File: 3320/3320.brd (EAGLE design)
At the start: 57.8 x 216.2 mm, 70 parts, among them IC1 OPA2134P, IC2 OPA2134P, X1 2516-

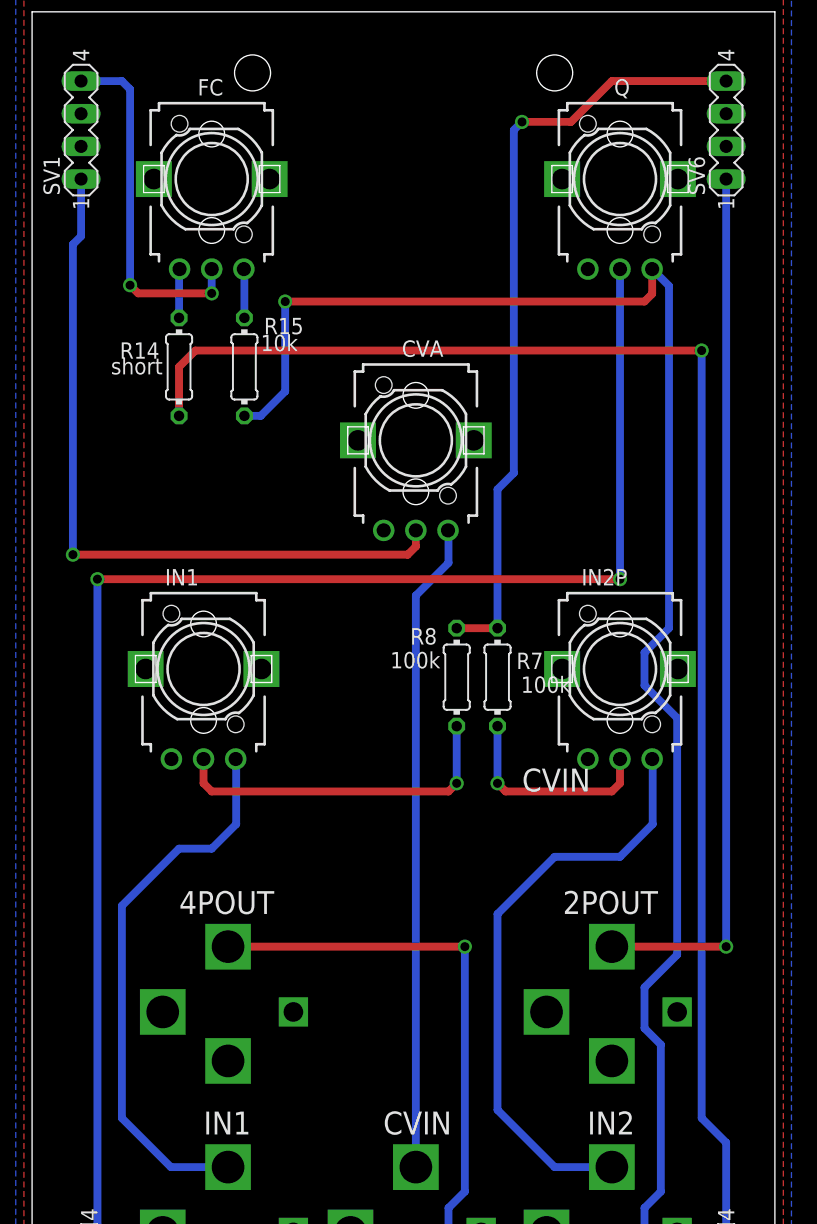
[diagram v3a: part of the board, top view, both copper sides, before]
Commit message: sent out vcf3 and 3320 for re spin
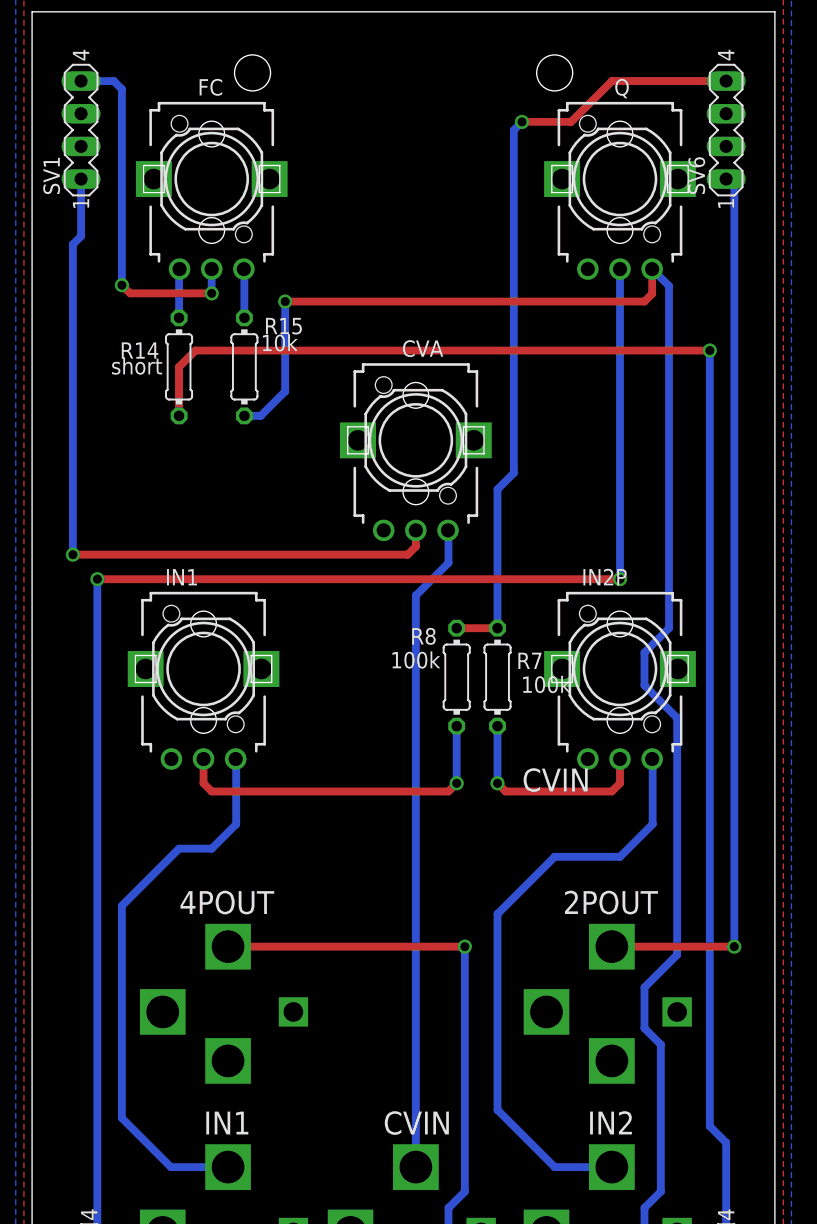
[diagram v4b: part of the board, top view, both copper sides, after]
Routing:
- net N$26: track 68.6 -> 69.5 mm
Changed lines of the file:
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@@
 <attribute name="VALUE" x="44.3992" y="31.4198" size="1.27" layer="21" font="vector" ratio="15"/>
 </element>
-<element name="IN1" library="dan" package="EVUFXJ" value="US-EVUF2J" x="13.335" y="165.1"/>
-<element name="IN2P" library="dan" package="EVUFXJ" value="US-EVUF2J" x="45.72" y="165.1"/>
+<element name="IN1" library="dan" package="EVUFXJ" value="US-EVUF2J" x="13.335" y="165.1" smashed="yes">
+<attribute name="NAME" x="10.335" y="171.6" size="1.27" layer="21"/>
+</element>
+<element name="IN2P" library="dan" package="EVUFXJ" value="US-EVUF2J" x="45.72" y="165.1" smashed="yes">
+<attribute name="NAME" x="42.72" y="171.6" size="1.27" layer="21"/>
+</element>
 </elements>
 <signals>
@@
 <contactref element="IC2" pad="4"/>
 <wire x1="53.975" y1="120.65" x2="53.975" y2="128.27" width="0.6096" layer="16"/>
-<wire x1="53.975" y1="128.27" x2="52.07" y2="130.175" width="0.6096" layer="16"/>
-<wire x1="52.07" y1="130.175" x2="52.07" y2="189.865" width="0.6096" layer="16"/>
-<via x="52.07" y="189.865" extent="1-16" drill="0.7"/>
+<wire x1="53.975" y1="128.27" x2="52.705" y2="129.54" width="0.6096" layer="16"/>
+<wire x1="52.705" y1="129.54" x2="52.705" y2="189.865" width="0.6096" layer="16"/>
+<via x="52.705" y="189.865" extent="1-16" drill="0.7"/>
 <contactref element="R27" pad="2"/>
 <contactref element="R26" pad="2"/>
@@
 <via x="41.275" y="12.065" extent="1-16" drill="0.7"/>
 <wire x1="41.275" y1="12.065" x2="45.085" y2="12.065" width="0.6096" layer="1"/>
-<wire x1="52.07" y1="189.865" x2="12.7" y2="189.865" width="0.6096" layer="1"/>
+<wire x1="52.705" y1="189.865" x2="12.7" y2="189.865" width="0.6096" layer="1"/>
 <wire x1="12.7" y1="189.865" x2="11.43" y2="188.595" width="0.6096" layer="1"/>
 <wire x1="11.43" y1="188.595" x2="11.43" y2="184.785" width="0.6096" layer="1"/>
@@
 <wire x1="13.97" y1="196.2" x2="13.97" y2="194.31" width="0.6096" layer="16"/>
 <via x="13.97" y="194.31" extent="1-16" drill="0.7"/>
-<wire x1="13.97" y1="194.31" x2="8.255" y2="194.31" width="0.6096" layer="1"/>
-<wire x1="8.255" y1="194.31" x2="7.62" y2="194.945" width="0.6096" layer="1"/>
-<via x="7.62" y="194.945" extent="1-16" drill="0.7"/>
-<wire x1="7.62" y1="194.945" x2="7.62" y2="210.185" width="0.6096" layer="16"/>
-<wire x1="7.62" y1="210.185" x2="6.985" y2="210.82" width="0.6096" layer="16"/>
-<wire x1="6.985" y1="210.82" x2="3.81" y2="210.82" width="0.6096" layer="16"/>
+<wire x1="13.97" y1="194.31" x2="7.62" y2="194.31" width="0.6096" layer="1"/>
+<wire x1="7.62" y1="194.31" x2="6.985" y2="194.945" width="0.6096" layer="1"/>
+<via x="6.985" y="194.945" extent="1-16" drill="0.7"/>
+<wire x1="6.985" y1="194.945" x2="6.985" y2="210.185" width="0.6096" layer="16"/>
+<wire x1="6.985" y1="210.185" x2="6.35" y2="210.82" width="0.6096" layer="16"/>
+<wire x1="6.35" y1="210.82" x2="3.81" y2="210.82" width="0.6096" layer="16"/>
 </signal>
 <signal name="N$17">
@@
 <contactref element="SV6" pad="1"/>
 <contactref element="2POUT" pad="P$3"/>
-<wire x1="53.975" y1="203.2" x2="53.975" y2="143.51" width="0.6096" layer="16"/>
-<via x="53.975" y="143.51" extent="1-16" drill="0.7"/>
-<wire x1="53.975" y1="143.51" x2="45.085" y2="143.51" width="0.6096" layer="1"/>
+<via x="54.61" y="143.51" extent="1-16" drill="0.7"/>
+<wire x1="54.61" y1="143.51" x2="45.085" y2="143.51" width="0.6096" layer="1"/>
+<wire x1="54.61" y1="143.51" x2="54.61" y2="202.565" width="0.6096" layer="16"/>
+<wire x1="54.61" y1="202.565" x2="53.975" y2="203.2" width="0.6096" layer="16"/>
 </signal>
 <signal name="N$28">

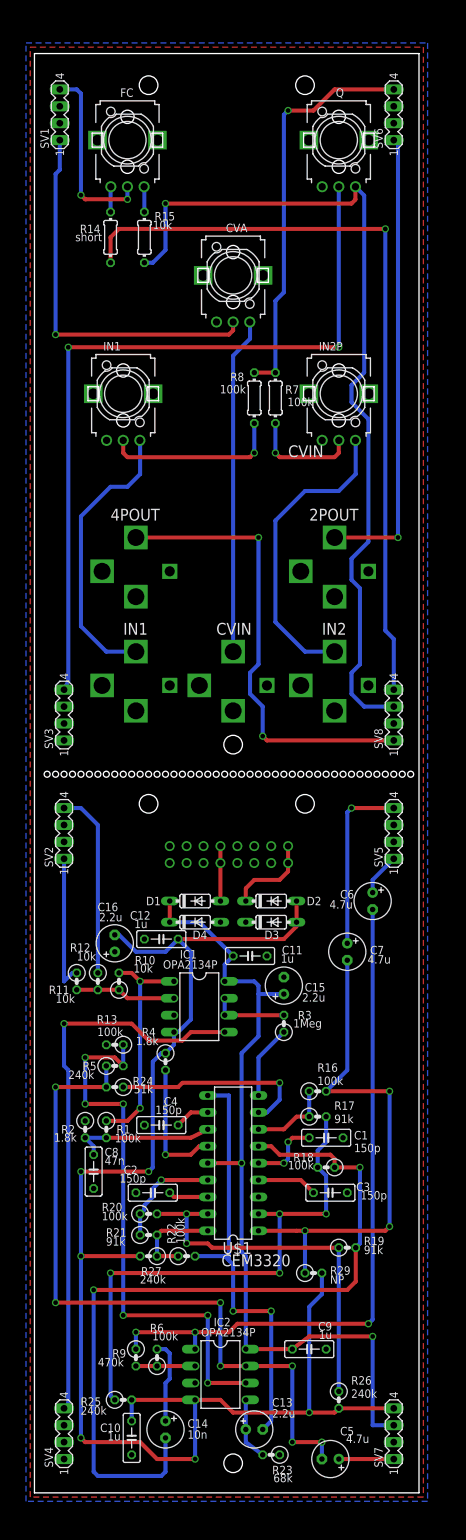
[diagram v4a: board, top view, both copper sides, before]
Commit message: made post fab component changes to 3320 and some fixes to svf board
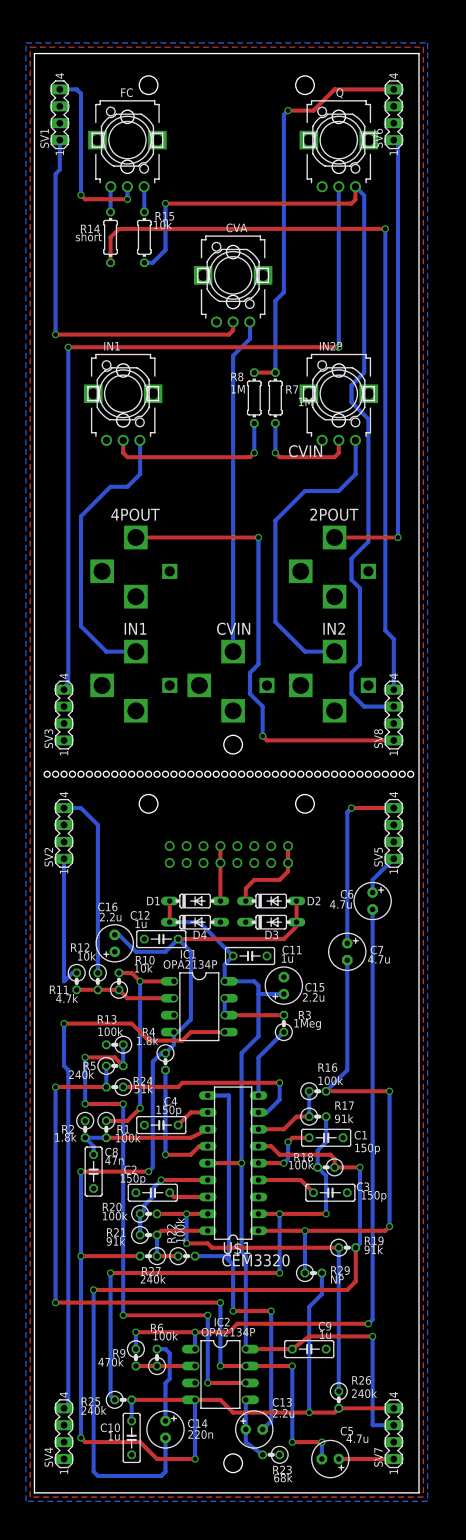
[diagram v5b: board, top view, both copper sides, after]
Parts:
- C14: value 10n -> 220n
- R11: value 10k -> 4.7k
- R7, R8: value 100k -> 1M
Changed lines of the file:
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@@
 <attribute name="VALUE" x="17.78" y="79.4258" size="1.27" layer="21" font="vector" ratio="15" rot="R180"/>
 </element>
-<element name="R11" library="dan" package="0207/2V" value="10k" x="6.35" y="76.835" smashed="yes" rot="R270">
+<element name="R11" library="dan" package="0207/2V" value="4.7k" x="6.35" y="76.835" smashed="yes" rot="R270">
 <attribute name="NAME" x="2.159" y="74.93" size="1.27" layer="21" font="vector" ratio="15"/>
 <attribute name="VALUE" x="3.175" y="73.6092" size="1.27" layer="21" font="vector" ratio="15"/>
@@
 <attribute name="VALUE" x="21.59" y="24.1808" size="1.27" layer="21" font="vector" ratio="15" rot="R180"/>
 </element>
-<element name="R7" library="dan" package="0204/7" value="100k" x="36.195" y="164.465" smashed="yes" rot="R90">
+<element name="R7" library="dan" package="0204/7" value="1M" x="36.195" y="164.465" smashed="yes" rot="R90">
 <attribute name="NAME" x="39.751" y="166.37" size="1.27" layer="21" font="vector" ratio="15" rot="R180"/>
 <attribute name="VALUE" x="41.91" y="164.5158" size="1.27" layer="21" font="vector" ratio="15" rot="R180"/>
 </element>
-<element name="R8" library="dan" package="0204/7" value="100k" x="33.02" y="164.465" smashed="yes" rot="R90">
+<element name="R8" library="dan" package="0204/7" value="1M" x="33.02" y="164.465" smashed="yes" rot="R90">
 <attribute name="NAME" x="31.496" y="168.275" size="1.27" layer="21" font="vector" ratio="15" rot="R180"/>
 <attribute name="VALUE" x="31.75" y="166.4208" size="1.27" layer="21" font="vector" ratio="15" rot="R180"/>
@@
 <attribute name="VALUE" x="19.7358" y="32.7152" size="1.27" layer="21" font="vector" ratio="15" rot="R180"/>
 </element>
-<element name="C14" library="dan" package="E2,5-6" value="10n" x="19.685" y="9.525" smashed="yes" rot="R270">
+<element name="C14" library="dan" package="E2,5-6" value="220n" x="19.685" y="9.525" smashed="yes" rot="R270">
 <attribute name="NAME" x="22.987" y="9.779" size="1.27" layer="21" font="vector" ratio="15"/>
 <attribute name="VALUE" x="22.987" y="8.128" size="1.27" layer="21" font="vector" ratio="15"/>

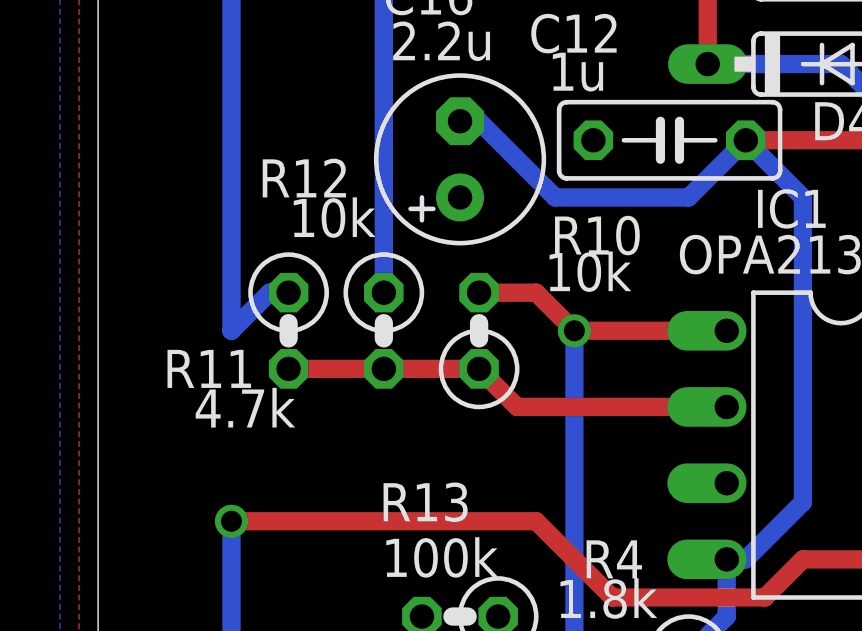
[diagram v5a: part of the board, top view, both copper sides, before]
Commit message: respun the svf.  changed a few components on the 3320
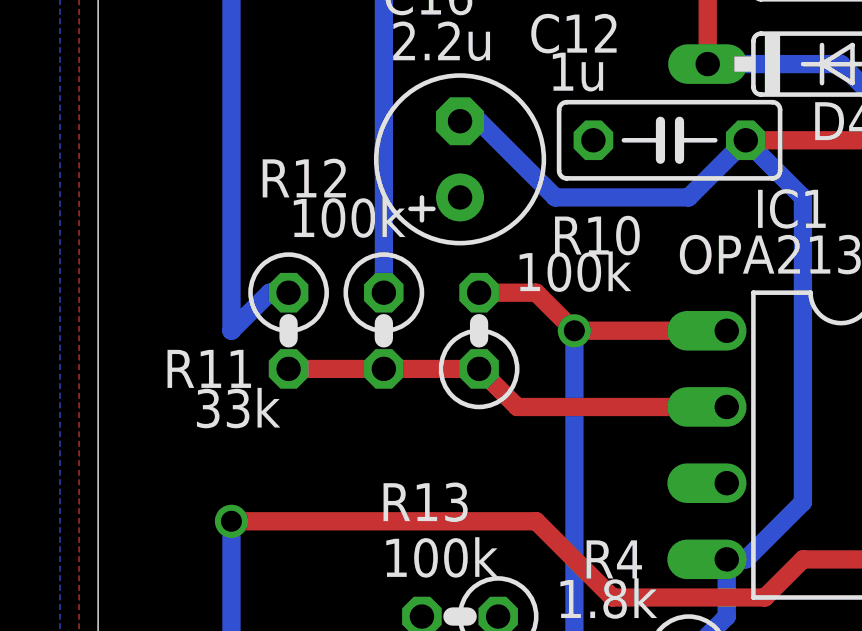
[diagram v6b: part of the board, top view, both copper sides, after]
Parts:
- R10, R12: value 10k -> 100k
- R11: value 4.7k -> 33k
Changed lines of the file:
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@@
 <attribute name="VALUE" x="12.065" y="52.6542" size="1.27" layer="21" font="vector" ratio="15"/>
 </element>
-<element name="R10" library="dan" package="0207/2V" value="10k" x="12.7" y="76.835" smashed="yes" rot="R90">
+<element name="R10" library="dan" package="0207/2V" value="100k" x="12.7" y="76.835" smashed="yes" rot="R90">
 <attribute name="NAME" x="18.161" y="80.645" size="1.27" layer="21" font="vector" ratio="15" rot="R180"/>
 <attribute name="VALUE" x="17.78" y="79.4258" size="1.27" layer="21" font="vector" ratio="15" rot="R180"/>
 </element>
-<element name="R11" library="dan" package="0207/2V" value="4.7k" x="6.35" y="76.835" smashed="yes" rot="R270">
+<element name="R11" library="dan" package="0207/2V" value="33k" x="6.35" y="76.835" smashed="yes" rot="R270">
 <attribute name="NAME" x="2.159" y="74.93" size="1.27" layer="21" font="vector" ratio="15"/>
 <attribute name="VALUE" x="3.175" y="73.6092" size="1.27" layer="21" font="vector" ratio="15"/>
 </element>
-<element name="R12" library="dan" package="0207/2V" value="10k" x="9.525" y="76.835" smashed="yes" rot="R270">
+<element name="R12" library="dan" package="0207/2V" value="100k" x="9.525" y="76.835" smashed="yes" rot="R270">
 <attribute name="NAME" x="5.334" y="81.28" size="1.27" layer="21" font="vector" ratio="15"/>
 <attribute name="VALUE" x="6.35" y="79.9592" size="1.27" layer="21" font="vector" ratio="15"/>
